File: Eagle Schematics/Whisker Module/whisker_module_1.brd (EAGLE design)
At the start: 100 x 80 mm, 135 parts, among them IC1 74LS14N, IC2 74LS14N, IC3 74LS14N, IC4 74LS14N, IC5 74LS14N, IC6 74LS14N, IC7 74LS14N, M1 CD74HCT151E, M2 CD74HCT151E, M3 CD74HCT151E, M4 CD74HCT151E, M5 CD74HCT151E, X1 22-23-2021, X10 22-23-2021, X11 22-23-2021, X12 22-23-2021, X13 22-23-2021, X14 22-23-2021, X15 22-23-2021, X16 22-23-2021, X17 22-23-2021, X18 22-23-2021, X19 22-23-2021, X2 22-23-2021, X20 22-23-2021, X21 22-23-2021, X22 22-23-2021, X23 22-23-2021, X24 22-23-2021, X25 22-23-2021, X26 22-23-2021, X27 22-23-2021, X28 22-23-2021, X29 22-23-2021, X3 22-23-2021, X30 22-23-2021, X31 22-23-2021, X32 22-23-2021, X33 22-23-2021, X34 22-23-2021, X35 22-23-2021, X36 22-23-2021, X37 22-23-2021, X38 22-23-2021, X39 22-23-2021, X4 22-23-2021, X40 22-23-2021, X5 22-23-2021, X6 22-23-2021, X7 22-23-2021, X8 22-23-2021, X9 22-23-2021

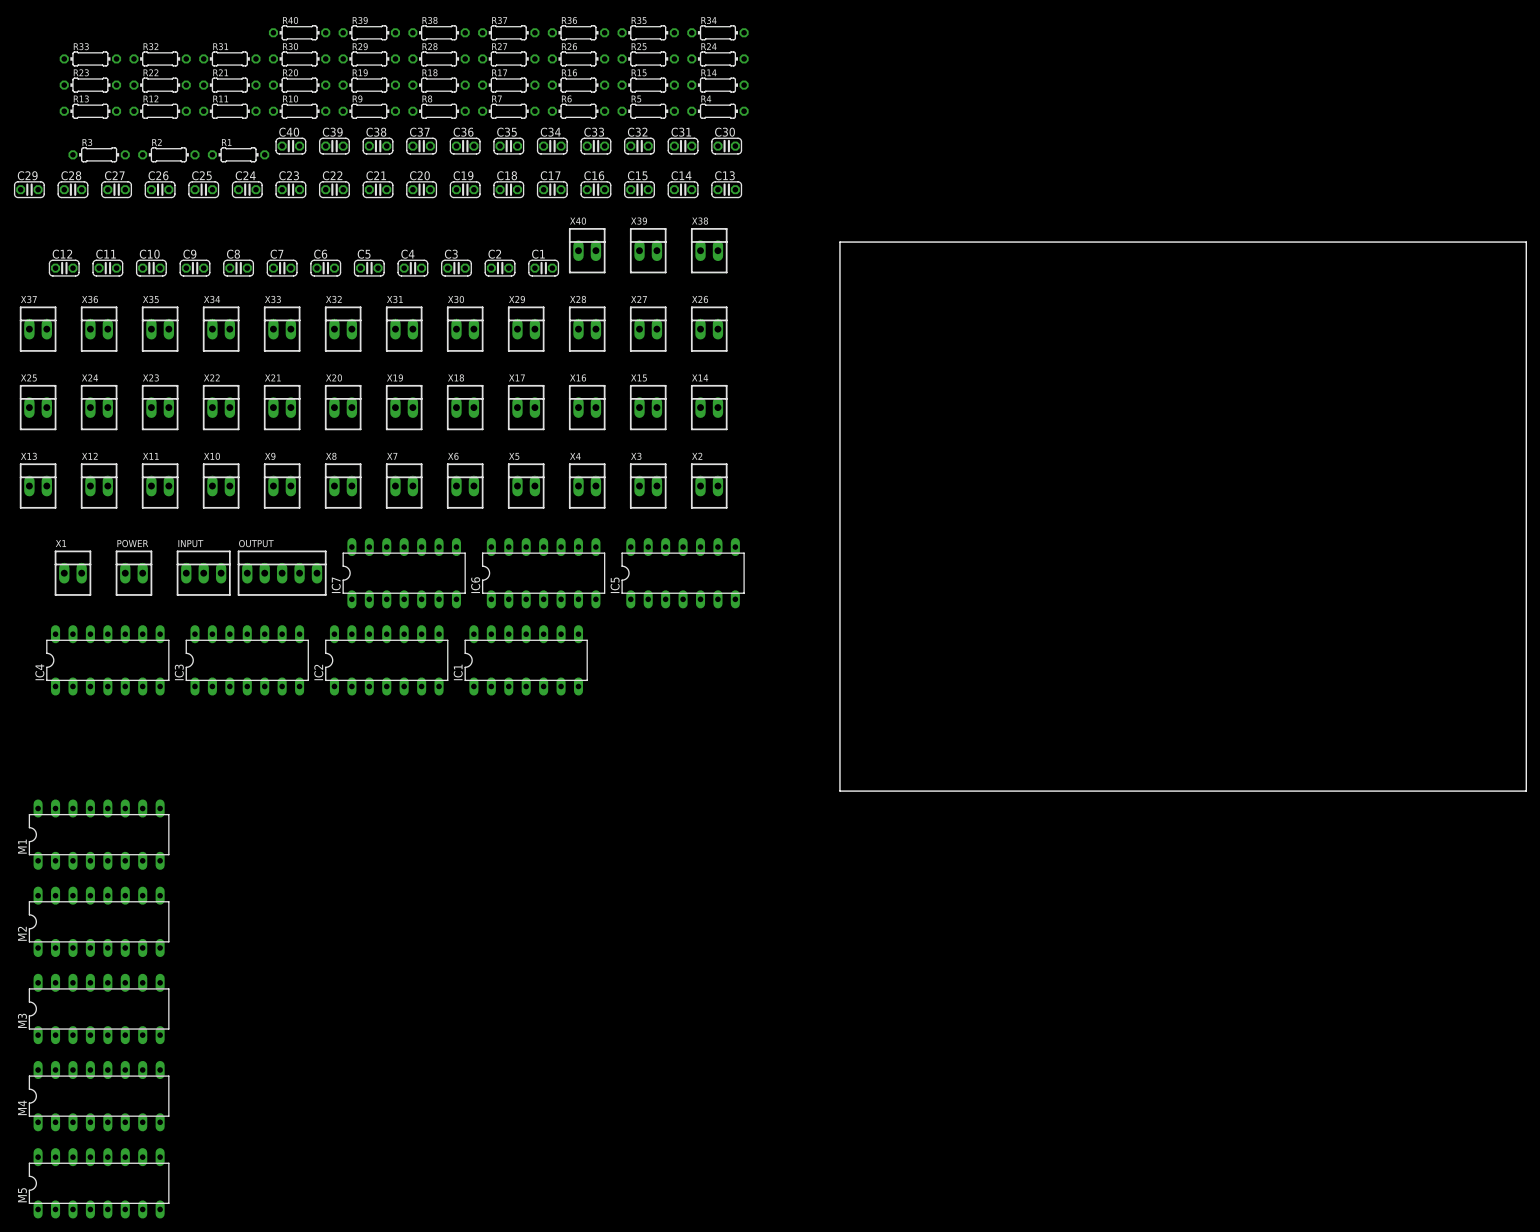
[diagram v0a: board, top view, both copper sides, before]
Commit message: Finished both whisker modules
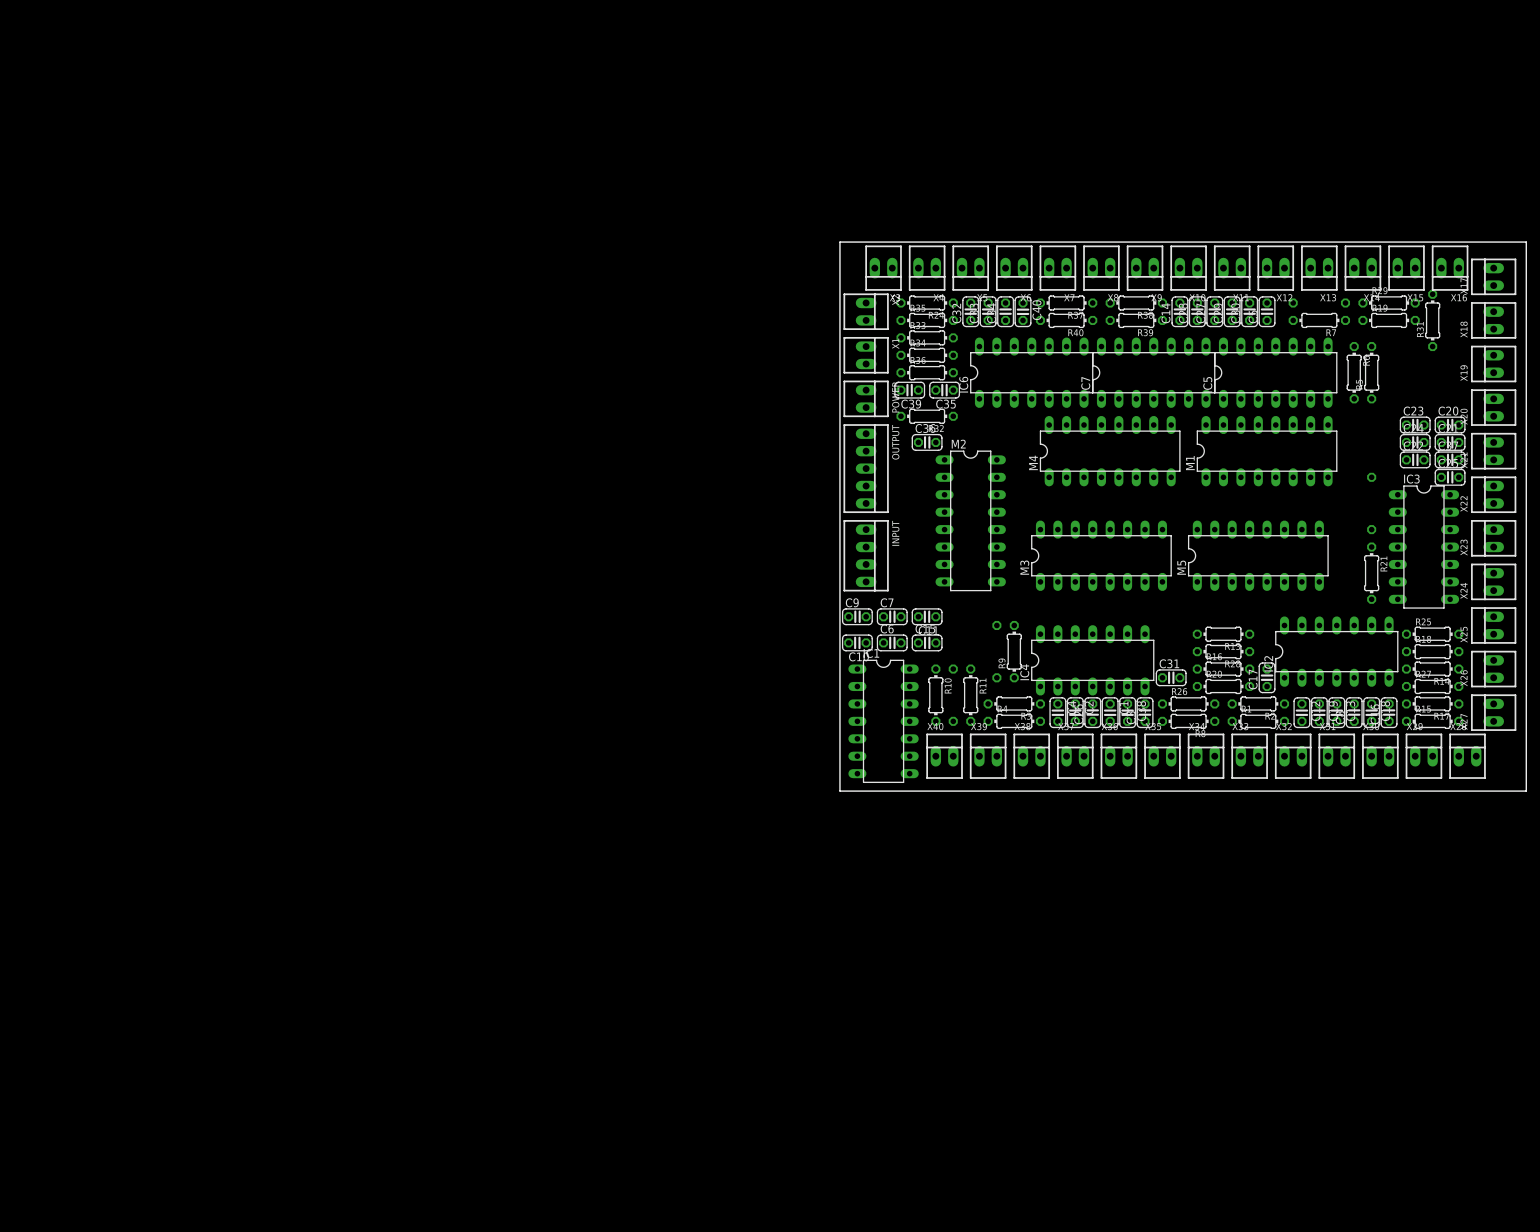
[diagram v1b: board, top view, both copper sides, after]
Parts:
- INPUT: value 22-23-2031 -> 22-23-2041; device con-molex:22-23-2031 -> con-molex:22-23-2041
- moved X25 214.5 mm to (95.2, 24.1), turned to 90 degrees
- moved X24 204.8 mm to (95.2, 30.5), turned to 90 degrees
- moved X23 195.2 mm to (95.2, 36.8), turned to 90 degrees
- moved M5 192.1 mm to (59.7, 34.3)
- moved C12 191.6 mm to (67.3, 11.4), turned to 270 degrees
- moved X13 189.4 mm to (69.8, 76.2), turned to 180 degrees
- moved R22 186.8 mm to (77.5, 41.9), flipped to the bottom, turned to 270 degrees
- moved C25 186.4 mm to (88.9, 45.7)
- moved X22 185.9 mm to (95.2, 43.2), turned to 90 degrees
- moved R13 181.8 mm to (55.9, 22.9), turned to 180 degrees
- moved R21 180.9 mm to (77.5, 31.8), turned to 270 degrees
- moved R31 179.4 mm to (86.4, 68.6), turned to 90 degrees
- moved M1 179.1 mm to (61.0, 49.5)
- moved R2 177.8 mm to (61.0, 12.7), turned to 180 degrees
- moved X21 176.6 mm to (95.2, 49.5), turned to 90 degrees
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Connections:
- new net SELECT4: INPUT.4, M1.7, M1.8, M2.7, M2.8, M3.7, M3.8, M4.7, M4.8, M5.7, M5.8
- net GND: no longer M1.7, M1.8, M2.7, M2.8, M3.7, M3.8, M4.7, M4.8, M5.7, M5.8
